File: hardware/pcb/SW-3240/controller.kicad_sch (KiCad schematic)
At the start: 30 parts, among them J2 USB_B_Micro, J3 ESPFlash, J4 JTAG, J5 I2C, Q1 S8050, Q2 S8050, SW1 RESET, SW2 BOOT, U1 CP2102N-A02-GQFN24, U2 ESP32-WROOM-32D

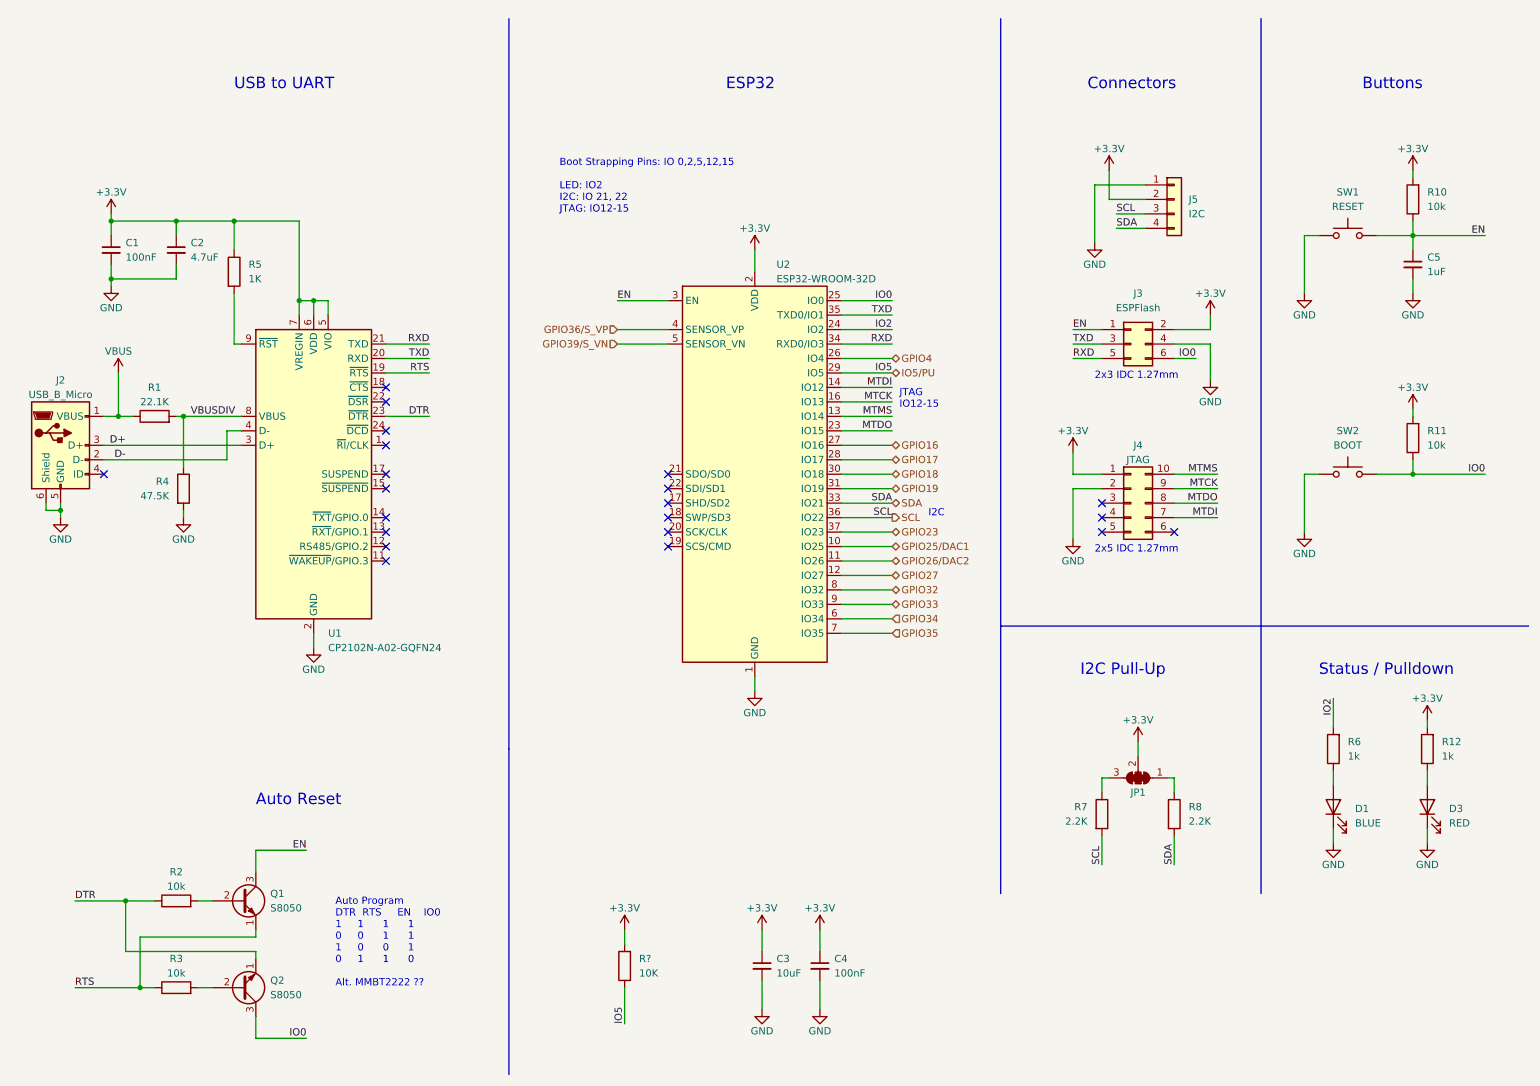
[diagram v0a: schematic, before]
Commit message: make SW-3240 modular
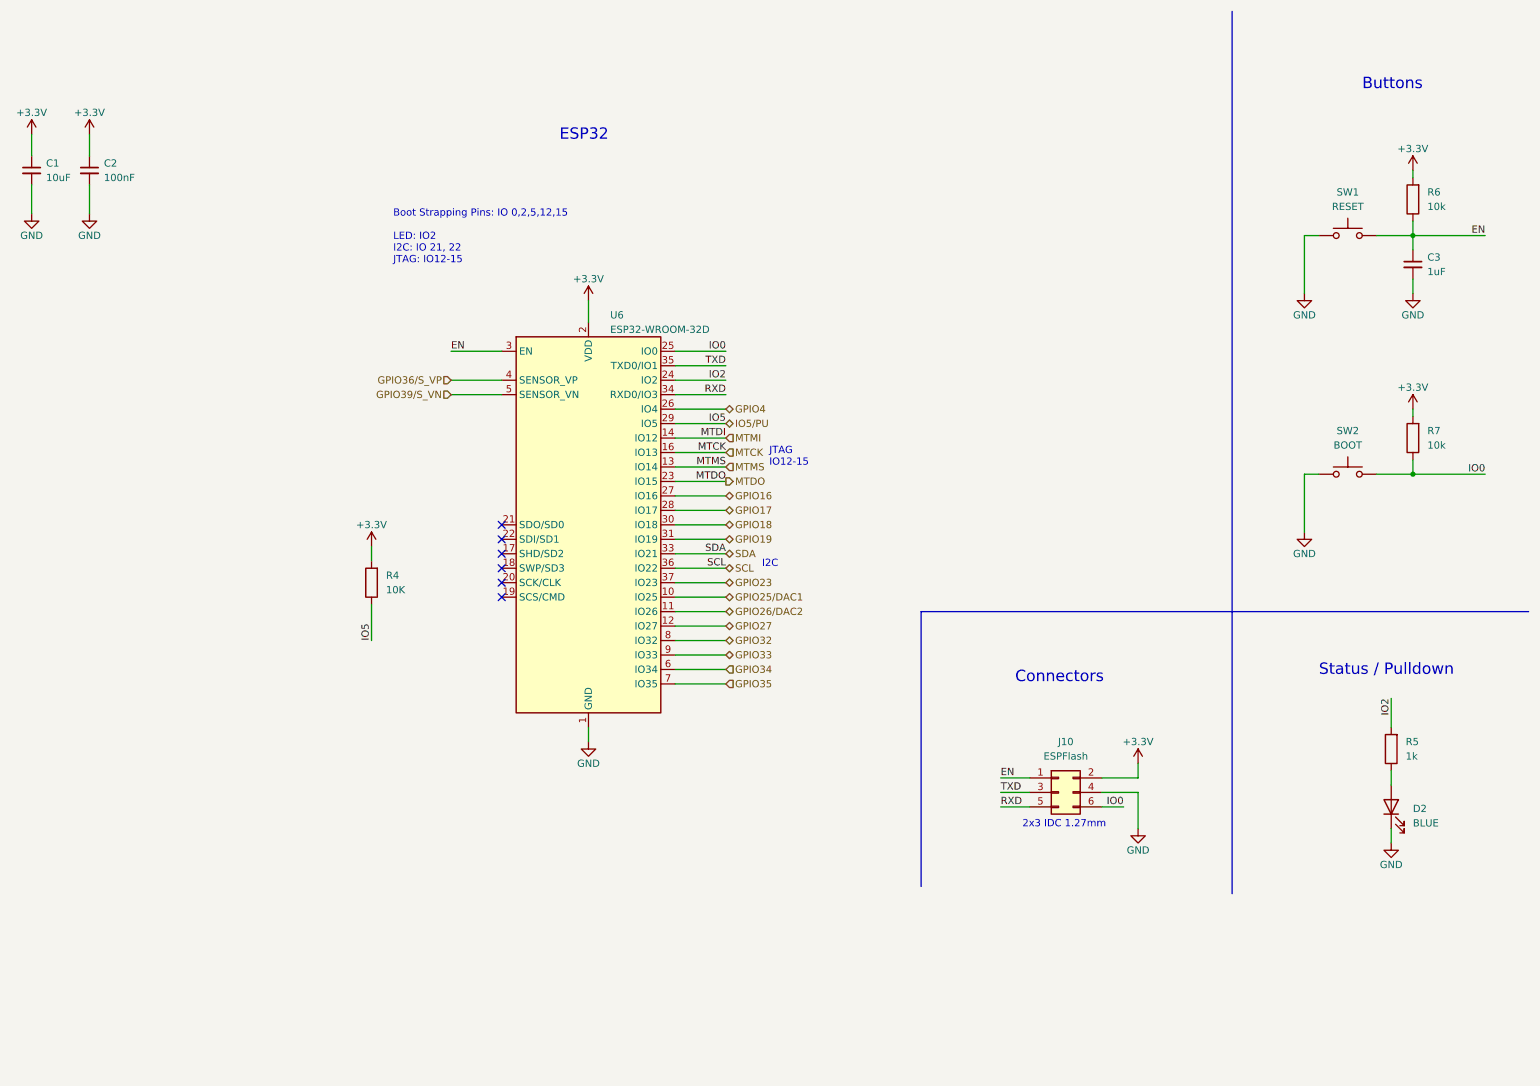
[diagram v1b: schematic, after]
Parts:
- removed C1: 100nF, Capacitor_SMD:C_0603_1608Metric, symbol Device:C_Small
- removed C2: 4.7uF, Capacitor_SMD:C_0603_1608Metric, symbol Device:C_Small
- removed D3: RED, LED_SMD:LED_0805_2012Metric, symbol Device:LED
- removed J2: USB_B_Micro, symbol Connector:USB_B_Micro
- removed J4: JTAG, symbol Connector_Generic:Conn_02x05_Counter_Clockwise
- removed J5: I2C, Connector_PinHeader_2.54mm:PinHeader_1x04_P2.54mm_Vertical, symbol Connector_Generic:Conn_01x04
- removed JP1: SolderJumper_3_Bridged123, symbol Jumper:SolderJumper_3_Bridged123
- removed Q1, Q2: S8050, Package_TO_SOT_SMD:SOT-23, symbol Transistor_BJT:S8050
- removed R1: 22.1K, Resistor_SMD:R_0603_1608Metric, symbol Device:R
- removed R12: 1k, Resistor_SMD:R_0603_1608Metric, symbol Device:R
- removed R2, R3: 10k, Resistor_SMD:R_0603_1608Metric, symbol Device:R
- removed R4: 47.5K, Resistor_SMD:R_0603_1608Metric, symbol Device:R
- removed R5: 1K, Resistor_SMD:R_0603_1608Metric, symbol Device:R
- removed R7, R8: 2.2K, Resistor_SMD:R_0603_1608Metric, symbol Device:R
- removed U1: CP2102N-A02-GQFN24, Package_DFN_QFN:QFN-24-1EP_4x4mm_P0.5mm_EP2.6x2.6mm, symbol Interface_USB:CP2102N-Axx-xQFN24
- J10: renamed from J3; footprint (none) -> Connector_PinHeader_1.27mm:PinHeader_2x03_P1.27mm_Vertical
- gave numbers to parts that had none: 1
- renumbered C3 to C1, C4 to C2, C5 to C3, D1 to D2, R6 to R5, R10 to R6, R11 to R7, U2 to U6
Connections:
- net MTDI renamed MTMI
- no-connect marks 21 -> 6
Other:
- note removed: "2x5 IDC 1.27mm"
- note removed: "Auto Program DTR RTS EN IO0 1 1 1 1 0 0 1 1 1 0 0 1 0 1 1 0 Alt. MMBT2222 ??"
- note removed: "Auto Reset"
- note removed: "I2C Pull-Up"
- note removed: "USB to UART"
- moved on the sheet: C1, C2, D2, J10, R4, R5, U6
